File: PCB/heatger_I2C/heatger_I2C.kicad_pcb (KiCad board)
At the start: 2 copper layers, 56 x 58 mm, 21 parts, among them J2 Screen, J3 BME280, SW3 Next, SW4 Order, U1 P82B715DR, U2 PCF8574

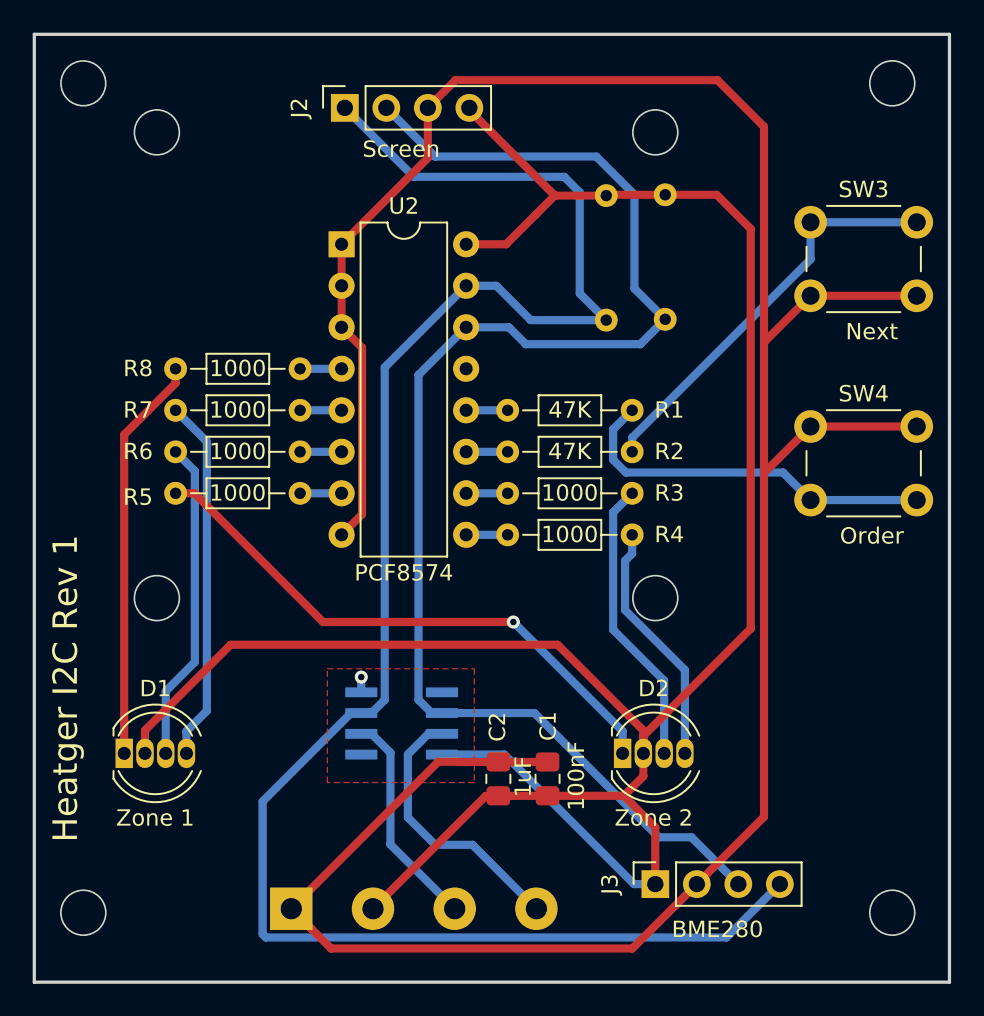
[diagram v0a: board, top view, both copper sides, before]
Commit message: add capacitors and gerbers files
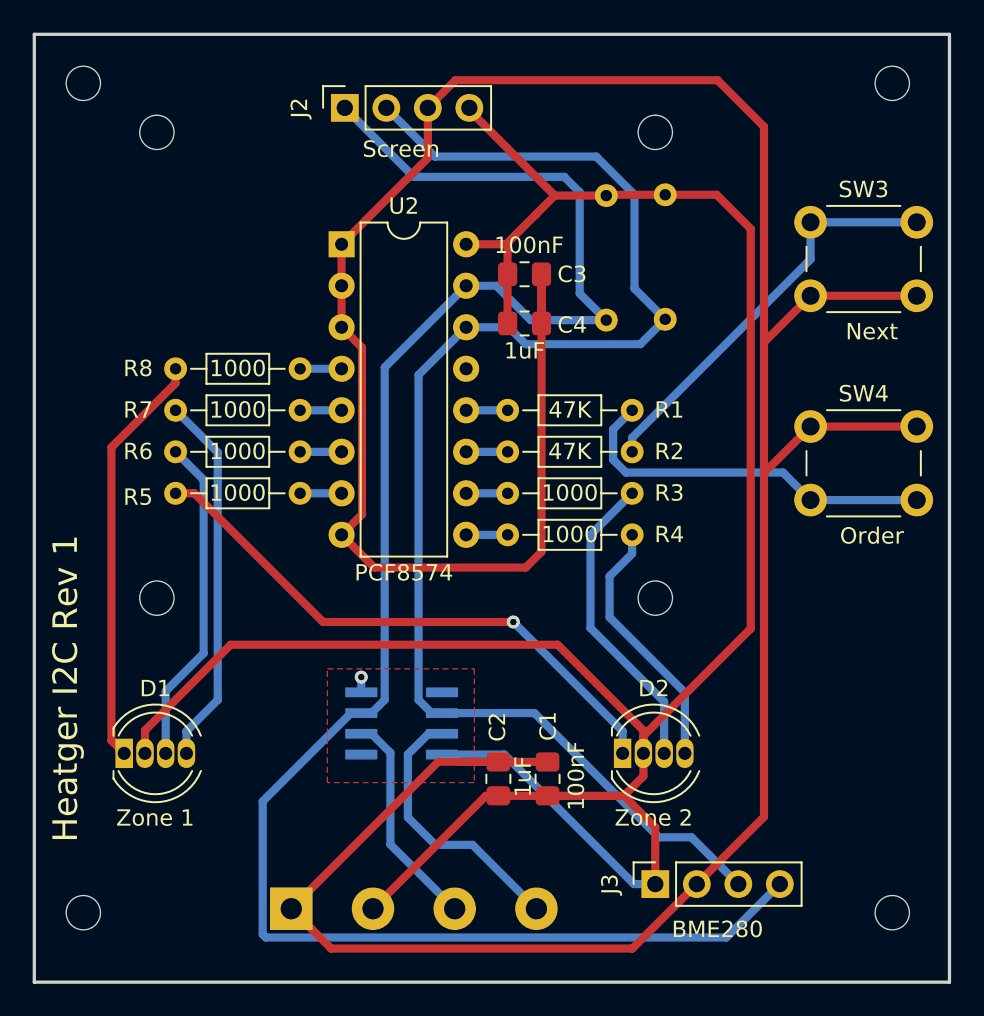
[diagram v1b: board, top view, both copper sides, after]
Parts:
- added C3: 100nF, Capacitor_SMD:C_0805_2012Metric_Pad1.18x1.45mm_HandSolder, F.Cu at (141.0, 53.7)
- added C4: 1uF, Capacitor_SMD:C_0805_2012Metric_Pad1.18x1.45mm_HandSolder, F.Cu at (141.0, 56.7)
- added REF**: MountingHole_2.1mm, MountingHole:MountingHole_2.1mm, F.Cu at (149.0, 73.5)
- added REF**: MountingHole_2.1mm, MountingHole:MountingHole_2.1mm, F.Cu at (114.0, 92.8)
- added REF**: MountingHole_2.1mm, MountingHole:MountingHole_2.1mm, F.Cu at (114.0, 42.0)
- added REF**: MountingHole_2.1mm, MountingHole:MountingHole_2.1mm, F.Cu at (149.0, 45.0)
- added REF**: MountingHole_2.1mm, MountingHole:MountingHole_2.1mm, F.Cu at (163.5, 92.8)
- added REF**: MountingHole_2.1mm, MountingHole:MountingHole_2.1mm, F.Cu at (118.5, 73.5)
- added REF**: MountingHole_2.1mm, MountingHole:MountingHole_2.1mm, F.Cu at (163.5, 42.0)
- added REF**: MountingHole_2.1mm, MountingHole:MountingHole_2.1mm, F.Cu at (118.5, 45.0)
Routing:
- net GND: track 170.4 -> 203.9 mm
- net +5V: track 143.4 -> 148.3 mm
- net Net-(D2-GK): track 17.7 -> 18.8 mm
- net Net-(D2-BK): track 15.1 -> 15.9 mm
- net Net-(D1-RK): track 24.8 -> 25.5 mm
- net Net-(D1-BK): track 22.3 -> 22.9 mm
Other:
- outline, holes or cut-outs redrawn

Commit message: invert wiring for pin headers
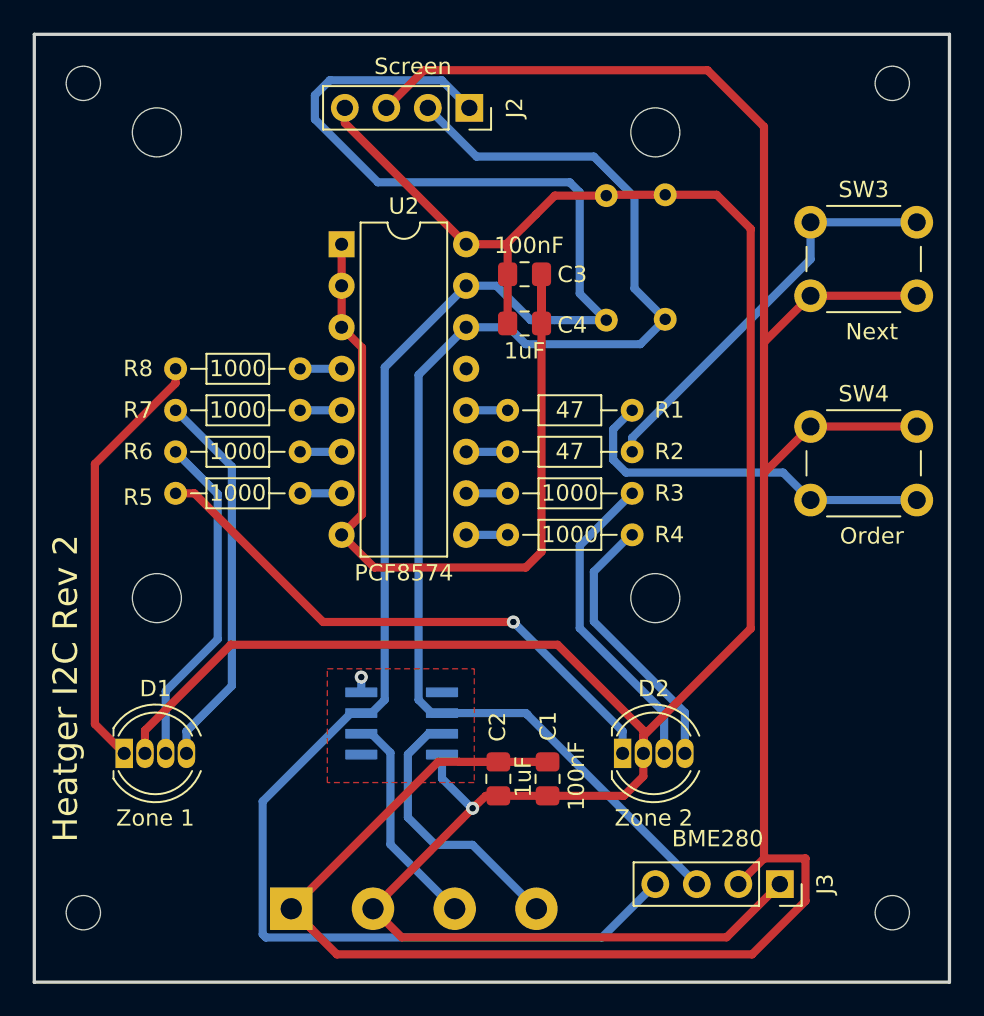
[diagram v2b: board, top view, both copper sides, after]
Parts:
- R1, R2: value 47K -> 47
- REF** (x4): value MountingHole_2.1mm -> MountingHole_3mm; footprint MountingHole:MountingHole_2.1mm -> MountingHole:MountingHole_3mm
- moved J2 7.62 mm to (137.6, 43.5), turned to -90 degrees
- moved J3 7.62 mm to (156.6, 91.0), turned to -90 degrees
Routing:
- net +5V: track 148.3 -> 160.6 mm, vias 0 -> 1
- net Net-(J2-Pin_1): track 113.1 -> 119.0 mm
- net Net-(J2-Pin_2): track 87.3 -> 82.1 mm
- net GND: track 203.9 -> 207.0 mm
- net Net-(D2-BK): track 15.9 -> 16.7 mm
- net Net-(D1-RK): track 25.5 -> 26.3 mm
- net Net-(D1-GK): track 20.1 -> 20.8 mm
- net Net-(D1-BK): track 22.9 -> 23.6 mm
- net Net-(D2-GK): track 18.8 -> 19.4 mm
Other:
- board text added: "Heatger I2C Rev 2"
- board text removed: "Heatger I2C Rev 1"

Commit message: add missing route
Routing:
- net GND: track 207.0 -> 216.2 mm
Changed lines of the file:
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@@
   (via (at 131.007 78.3319) (size 0.8) (drill 0.4) (layers "F.Cu" "B.Cu") (net 8))
   (segment (start 131.007 79.264) (end 131.007 78.3319) (width 0.5) (layer "B.Cu") (net 8))
+  (segment (start 129.804 77.1289) (end 129.804 69.627) (width 0.5) (layer "B.Cu") (net 8))
+  (segment (start 131.007 78.3319) (end 129.804 77.1289) (width 0.5) (layer "B.Cu") (net 8))
   (segment (start 132.0292 48.0568) (end 128.1684 44.196) (width 0.5) (layer "B.Cu") (net 9))
   (segment (start 131.007 80.534) (end 131.634 80.534) (width 0.5) (layer "B.Cu") (net 9))
